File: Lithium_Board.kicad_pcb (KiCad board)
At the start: 6 copper layers, 80 x 67 mm, 120 parts, among them IC1 BQ25750RRVR, IC2 MCP1792T-3302H_DB, IC4 STM32G0B1CBT6N, IC5 TCAN3414DR, IC6 BQ7694204PFBR, J1 XT30PW-M, J2 XT30PW-F, J3 XT30PW-M, J4 S3B-XH-SM4-TB_LF__SN_, J5 TSW-105-07-G-S, J6 Conn_01x06, J7 Conn_01x04, Q1 SIR870ADP-T1-GE3, Q10 MMBT5551LT1G, Q2 SIR870ADP-T1-GE3, Q3 SIR870ADP-T1-GE3, Q4 SIR870ADP-T1-GE3, Q5 SIR870ADP-T1-GE3, Q6 SIR870ADP-T1-GE3, Q7 SIR870ADP-T1-GE3, Q8 SIR870ADP-T1-GE3

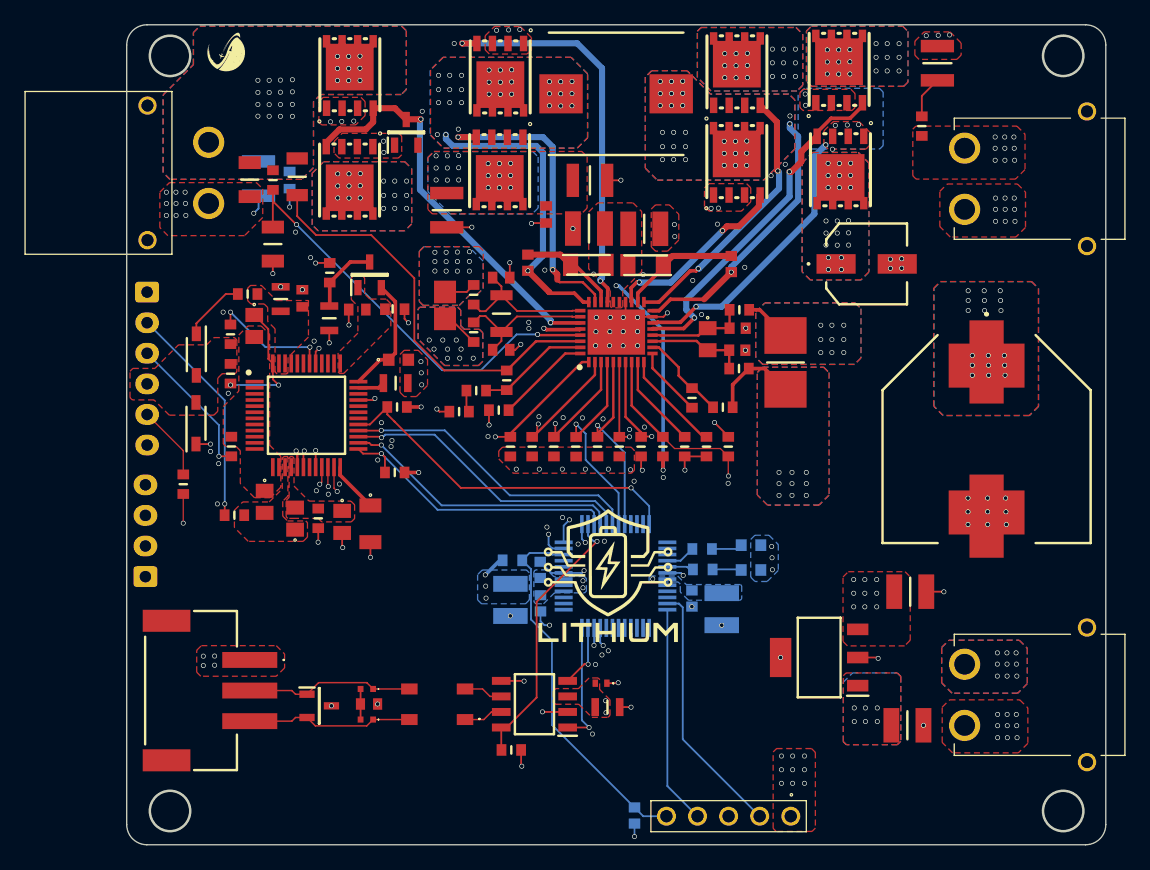
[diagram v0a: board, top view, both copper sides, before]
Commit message: Fixed Mounting Holes
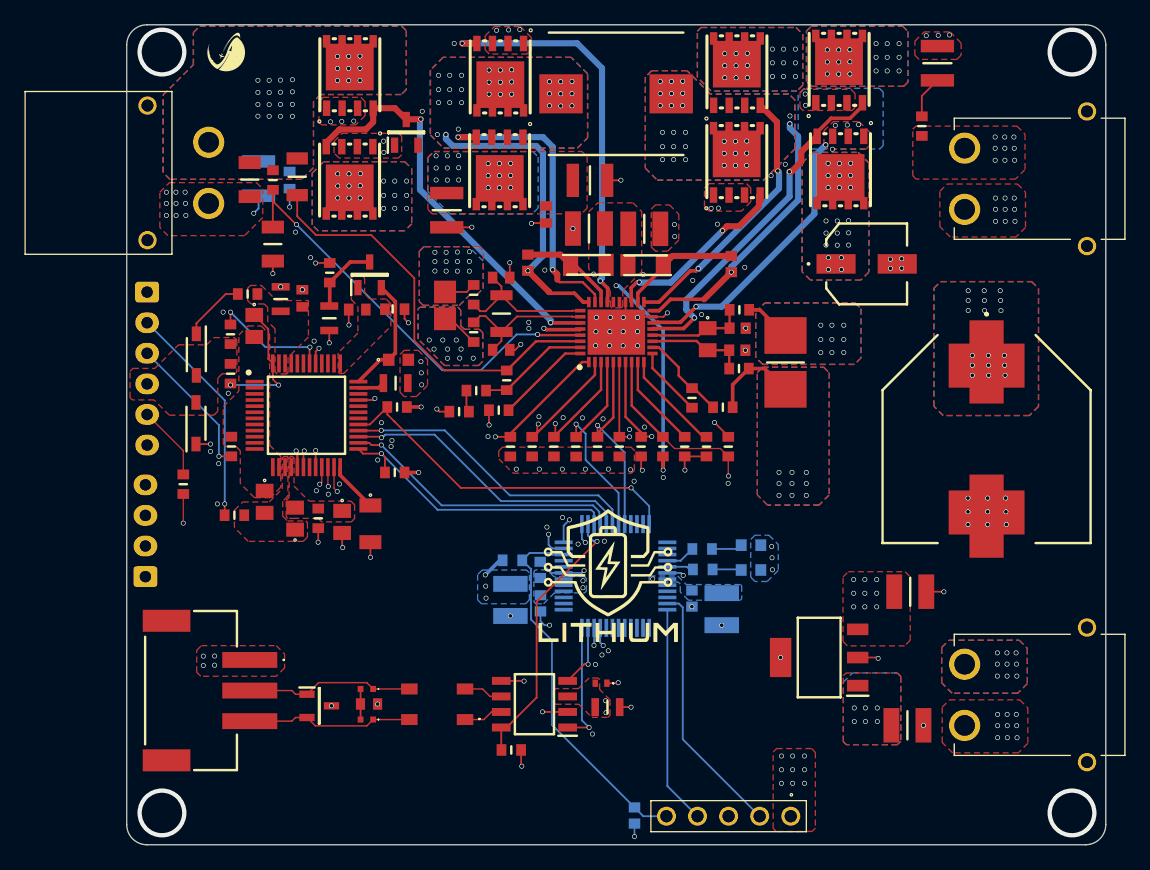
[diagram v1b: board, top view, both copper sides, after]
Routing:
- net GND: vias 171 -> 175
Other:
- outline, holes or cut-outs redrawn
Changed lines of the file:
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@@
 		(embedded_fonts no)
-	)
-	(gr_circle
-		(center 180.48 125.71)
-		(end 182.13 125.71)
-		(stroke
-			(width 0.2)
-			(type solid)
-		)
-		(fill no)
-		(layer "Edge.Cuts")
-	)
-	(gr_circle
-		(center 180.48 64.01)
-		(end 182.13 64.01)
-		(stroke
-			(width 0.2)
-			(type solid)
-		)
-		(fill no)
-		(layer "Edge.Cuts")
 	)
 	(gr_arc
@@
 		(layer "Edge.Cuts")
 	)
-	(gr_circle
-		(center 107.5 64.01)
-		(end 109.15 64.01)
-		(stroke
-			(width 0.2)
-			(type solid)
-		)
-		(fill no)
-		(layer "Edge.Cuts")
-	)
 	(gr_arc
 		(start 105.61 128.47)
@@
 			(type default)
 		)
-		(layer "Edge.Cuts")
-	)
-	(gr_circle
-		(center 107.5 125.71)
-		(end 109.15 125.71)
-		(stroke
-			(width 0.2)
-			(type solid)
-		)
-		(fill no)
 		(layer "Edge.Cuts")
 	)
@@
 	)
 	(via
+		(at 181.2 125.87)
+		(size 4)
+		(drill 3.3)
+		(layers "F.Cu" "B.Cu")
+		(free yes)
+		(tenting none)
+		(net 1)
+	)
+	(via
 		(at 176.48 75.63)
 		(size 0.4)
@@
 	)
 	(via
+		(at 106.84 63.7)
+		(size 4)
+		(drill 3.3)
+		(layers "F.Cu" "B.Cu")
+		(free yes)
+		(tenting none)
+		(net 1)
+	)
+	(via
 		(at 175.745 77.53)
 		(size 0.4)
@@
 	)
 	(via
+		(at 106.84 125.87)
+		(size 4)
+		(drill 3.3)
+		(layers "F.Cu" "B.Cu")
+		(free yes)
+		(tenting none)
+		(net 1)
+	)
+	(via
 		(at 158.151205 68.920096)
 		(size 0.4)
@@
 		(net 1)
 	)
+	(via
+		(at 181.2 63.7)
+		(size 4)
+		(drill 3.3)
+		(layers "F.Cu" "B.Cu")
+		(free yes)
+		(tenting none)
+		(net 1)
+	)

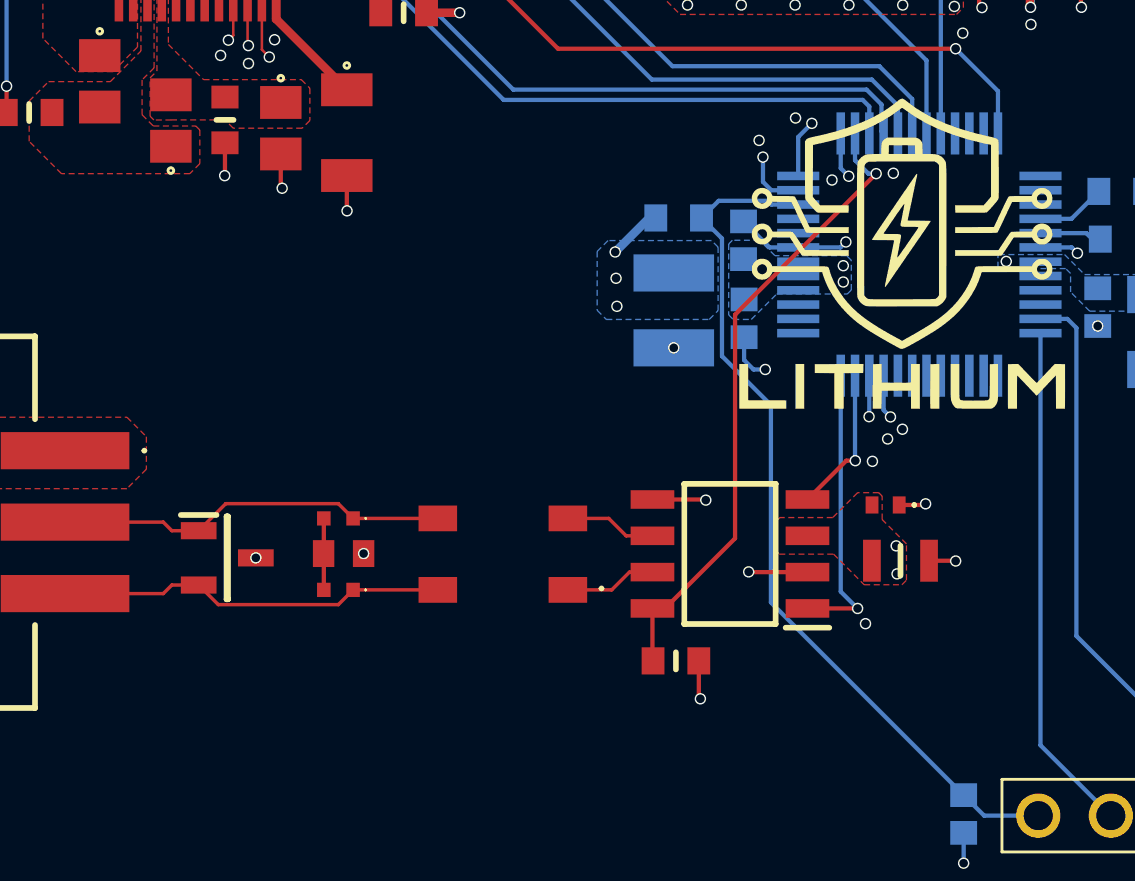
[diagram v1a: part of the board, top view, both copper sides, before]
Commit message: Fixed Items Not in Stock
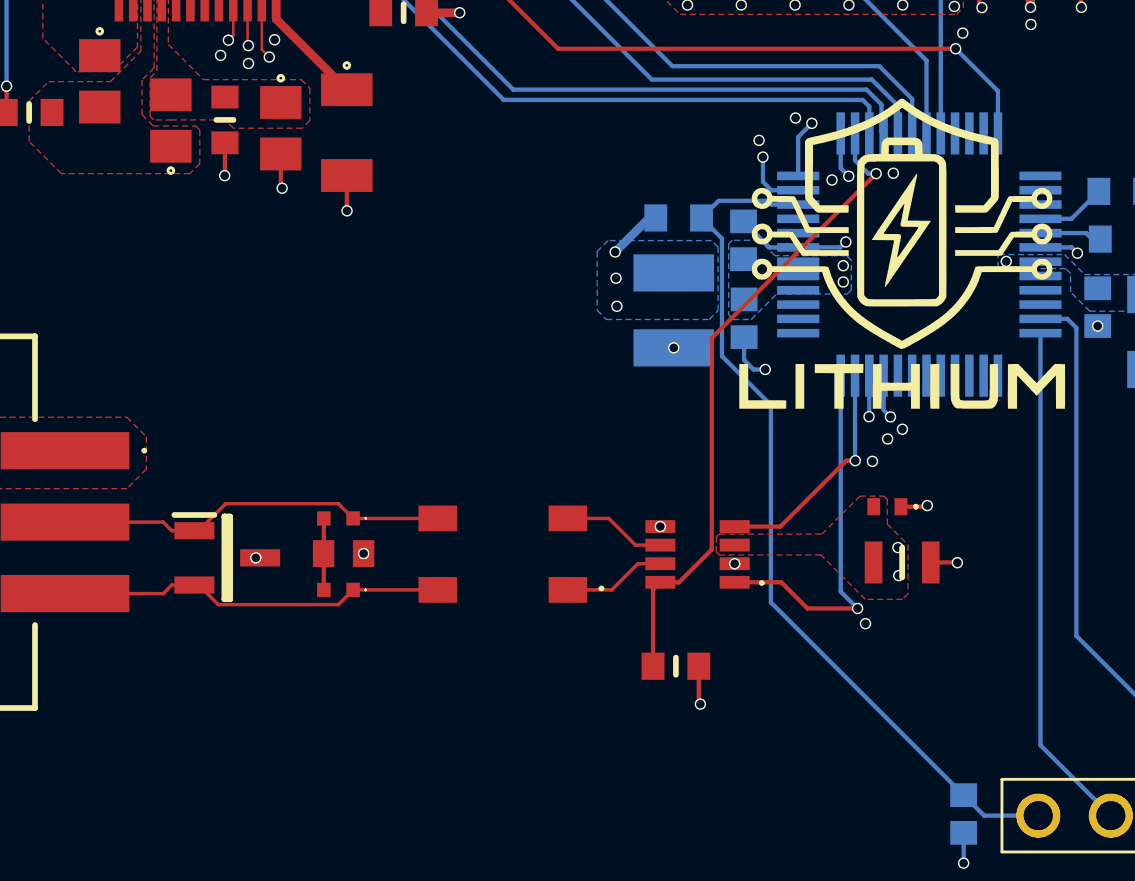
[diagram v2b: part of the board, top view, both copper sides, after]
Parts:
- removed IC5: TCAN3414DR, TCAN3414DR:SOIC127P600X175-8N
- added IC3: TCAN3414DDFR, TCAN3414DDFR:INA190A2NDDFREP, F.Cu at (136.1, 117.0)
- D1: value CDSOT23-T24CAN -> ESDCAN24-2BLY; footprint CDSOT23-T24CAN:SOT95P230X117-3N -> ESDCAN24-2BLY:SOT95P255X125-3N
- IC4: value STM32G0B1CBT6N -> STM32G0B1CET6N
- moved R35 0.19 mm to (135.4, 120.9)
- moved C25 0.08 mm to (142.8, 115.3)
- moved C26 0.08 mm to (143.3, 117.3)
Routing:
- net GND: track 61.2 -> 57.3 mm
- net FDCAN_RX: track 5.21 -> 8.15 mm
- net FDCAN_TX: track 10.1 -> 13.1 mm

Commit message: New BOM+GRB
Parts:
- IC4: footprint STM32G0B1CBT6N:QFP50P900X900X160-48N -> STM32G0B1CET6N:QFP50P900X900X160-48N
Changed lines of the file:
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@@
 		(tags "TVS Diode (Bi-directional)")
 		(property "Reference" "D1"
-			(at 0 0 -0)
+			(at 0 0 0)
 			(layer "B.SilkS")
 			(effects
@@
 		)
 		(fp_text user "${REFERENCE}"
-			(at 0 0 -0)
+			(at 0 0 0)
 			(layer "B.Fab")
 			(effects
@@
 		(tags "Integrated Circuit")
 		(property "Reference" "IC3"
-			(at 0 0 -0)
+			(at 0 0 0)
 			(layer "B.SilkS")
 			(effects
@@
 		)
 		(fp_text user "${REFERENCE}"
-			(at 0 0 -0)
+			(at 0 0 0)
 			(layer "B.Fab")
 			(effects
@@
 		)
 	)
-	(footprint "STM32G0B1CBT6N:QFP50P900X900X160-48N"
+	(footprint "STM32G0B1CET6N:QFP50P900X900X160-48N"
 		(layer "B.Cu")
 		(at 143.9 106.509999)
-		(descr "LQFP48 package information (5B)-1")
+		(descr "ANT1204F007R0870A")
 		(tags "Integrated Circuit")
 		(property "Reference" "IC4"
@@
 		)
 		(embedded_fonts no)
-		(model "${KIPRJMOD}/Lithium_Footprints/LIB_STM32G0B1CBT6N/STM32G0B1CBT6N/3D/STM32G0B1CBT6N.stp"
+		(model "STM32G0B1CET6N.stp"
 			(offset
 				(xyz 0 0 0)

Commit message: BOM Fixed+CS Fixed
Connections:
- IC4 pad 24: BQ2_CS -> unconnected-(IC4-PB12-Pad24)
- IC4 pad 37: unconnected-(IC4-PA15-Pad37) -> BQ2_CS
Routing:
- net BQ2_CS: track 29.5 -> 40.2 mm
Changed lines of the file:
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@@
 	(net 113 "unconnected-(IC4-PA11_[PA9]-Pad33)")
 	(net 114 "LED2_GREEN")
-	(net 115 "unconnected-(IC4-PA15-Pad37)")
+	(net 115 "unconnected-(IC4-PB12-Pad24)")
 	(net 116 "LED1_RED")
 	(net 117 "unconnected-(IC4-PD0-Pad38)")
@@
 			(size 0.3 1.475)
 			(layers "B.Cu" "B.Mask" "B.Paste")
-			(net 55 "BQ2_CS")
+			(net 115 "unconnected-(IC4-PB12-Pad24)")
 			(pinfunction "PB12")
-			(pintype "passive")
+			(pintype "passive+no_connect")
 		)
 		(pad "25" smd rect
@@
 			(size 0.3 1.475)
 			(layers "B.Cu" "B.Mask" "B.Paste")
-			(net 115 "unconnected-(IC4-PA15-Pad37)")
+			(net 55 "BQ2_CS")
 			(pinfunction "PA15")
-			(pintype "passive+no_connect")
+			(pintype "passive")
 		)
 		(pad "38" smd rect
@@
 	)
 	(segment
+		(start 148.613 109.8)
+		(end 147.663 110.75)
+		(width 0.15)
+		(layer "F.Cu")
+		(net 55)
+	)
+	(segment
 		(start 145.17 99.31)
 		(end 131.26 99.31)
@@
 	)
 	(segment
+		(start 148.613 102.753)
+		(end 148.613 109.8)
+		(width 0.15)
+		(layer "F.Cu")
+		(net 55)
+	)
+	(segment
+		(start 145.17 99.31)
+		(end 148.613 102.753)
+		(width 0.15)
+		(layer "F.Cu")
+		(net 55)
+	)
+	(segment
 		(start 131.26 99.31)
 		(end 125.84 93.89)
@@
 	)
 	(via
-		(at 145.17 99.31)
+		(at 147.663 110.75)
 		(size 0.4)
 		(drill 0.3)
 		(layers "F.Cu" "B.Cu")
-		(tenting front back)
 		(net 55)
 	)
 	(segment
-		(start 146.65 102.271999)
-		(end 146.65 100.79)
+		(start 146.652001 110.75)
+		(end 146.65 110.747999)
 		(width 0.15)
 		(layer "B.Cu")
@@
 	)
 	(segment
-		(start 146.65 100.79)
-		(end 145.17 99.31)
+		(start 147.663 110.75)
+		(end 146.652001 110.75)
 		(width 0.15)
 		(layer "B.Cu")

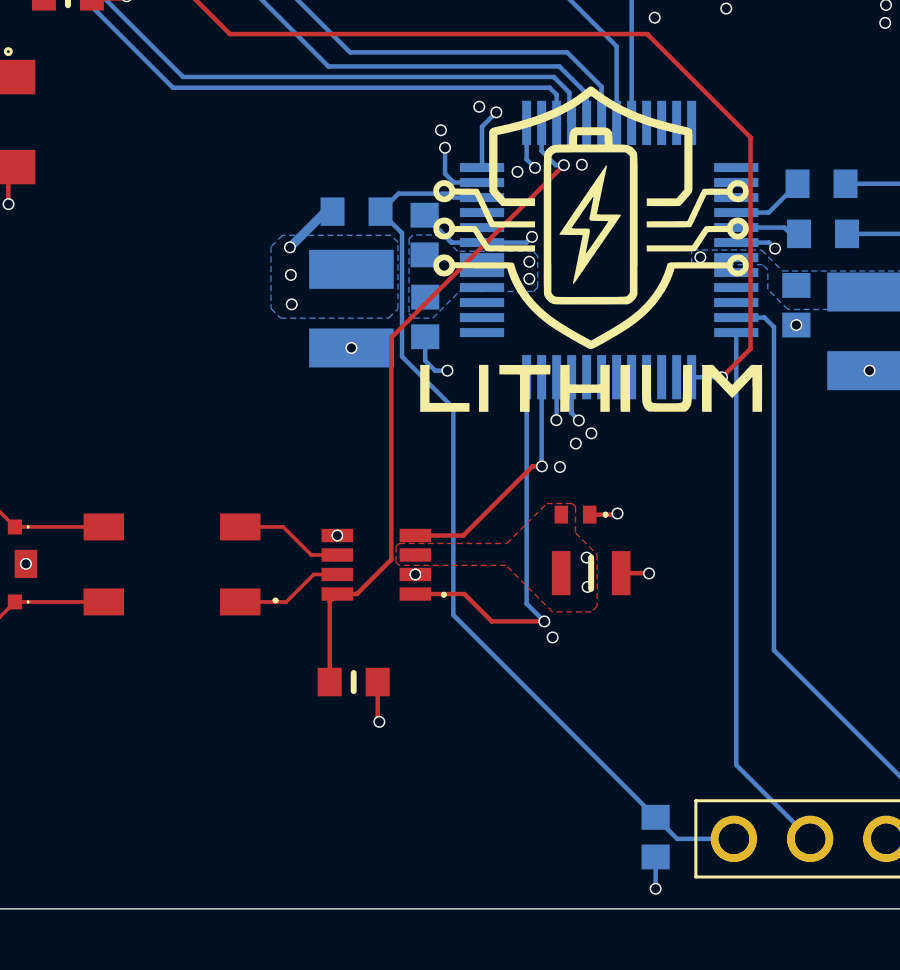
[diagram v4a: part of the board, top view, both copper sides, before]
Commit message: NRST+Polygon Fixed
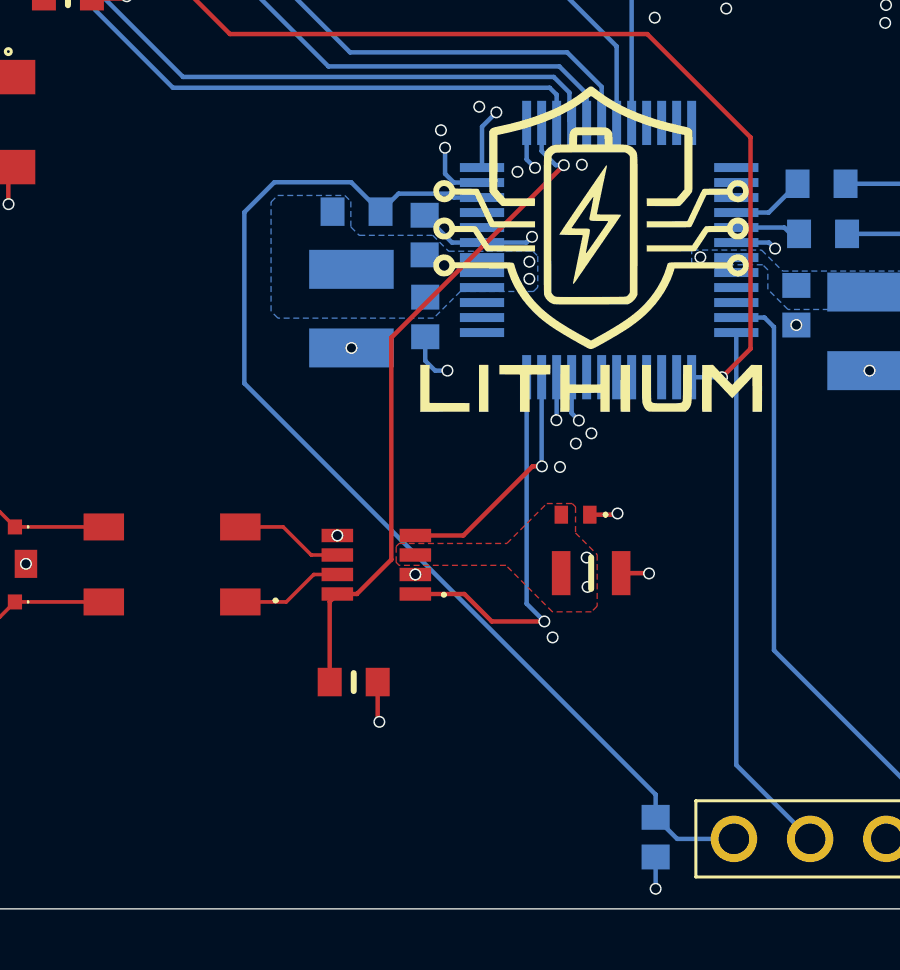
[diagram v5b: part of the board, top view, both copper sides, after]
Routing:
- net NRST: track 30.6 -> 37.8 mm
- net +3V3: track 4.24 -> 2.33 mm, vias 34 -> 31
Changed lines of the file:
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@@
 	)
 	(via
-		(at 133.32 108.32)
-		(size 0.4)
-		(drill 0.3)
-		(layers "F.Cu" "B.Cu")
-		(free yes)
-		(tenting front back)
-		(net 12)
-	)
-	(via
 		(at 163.36 106.8)
 		(size 0.4)
@@
 	)
 	(via
-		(at 133.26 106.42)
-		(size 0.4)
-		(drill 0.3)
-		(layers "F.Cu" "B.Cu")
-		(free yes)
-		(tenting front back)
-		(net 12)
-	)
-	(via
 		(at 137.672 97.78)
 		(size 0.4)
@@
 	)
 	(via
-		(at 133.29 107.34)
-		(size 0.4)
-		(drill 0.3)
-		(layers "F.Cu" "B.Cu")
-		(free yes)
-		(tenting front back)
-		(net 12)
-	)
-	(via
 		(at 158.37 121.22)
 		(size 0.4)
@@
 	)
 	(segment
-		(start 134.45 105.23)
-		(end 133.26 106.42)
-		(width 0.3)
-		(layer "B.Cu")
-		(net 12)
-	)
-	(segment
-		(start 134.68 105.23)
-		(end 134.45 105.23)
-		(width 0.3)
-		(layer "B.Cu")
-		(net 12)
-	)
-	(segment
 		(start 154.79 89.56)
 		(end 156.088225 89.56)
@@
 	)
 	(segment
-		(start 138.707166 118.677166)
-		(end 138.707166 111.774165)
+		(start 148.06 126.1375)
+		(end 146.1675 126.1375)
 		(width 0.15)
 		(layer "B.Cu")
@@
 	)
 	(segment
-		(start 136.996 110.062999)
-		(end 136.996 105.946)
+		(start 145.45 124.661834)
+		(end 145.45 125.42)
 		(width 0.15)
 		(layer "B.Cu")
@@
 	)
 	(segment
-		(start 138.707166 111.774165)
-		(end 136.996 110.062999)
+		(start 131.74 110.951834)
+		(end 145.45 124.661834)
 		(width 0.15)
 		(layer "B.Cu")
@@
 	)
 	(segment
-		(start 148.06 126.1375)
-		(end 146.1675 126.1375)
+		(start 136.28 105.23)
+		(end 136.88 104.63)
 		(width 0.15)
 		(layer "B.Cu")
@@
 	)
 	(segment
-		(start 136.28 105.23)
-		(end 136.88 104.63)
+		(start 146.1675 126.1375)
+		(end 145.45 125.42)
 		(width 0.15)
 		(layer "B.Cu")
@@
 	)
 	(segment
-		(start 146.1675 126.1375)
-		(end 145.45 125.42)
+		(start 136.88 104.63)
+		(end 138.592501 104.63)
 		(width 0.15)
 		(layer "B.Cu")
@@
 	)
 	(segment
-		(start 145.45 125.42)
-		(end 138.707166 118.677166)
+		(start 131.74 105.25)
+		(end 131.74 110.951834)
 		(width 0.15)
 		(layer "B.Cu")
@@
 	)
 	(segment
-		(start 136.88 104.63)
-		(end 138.592501 104.63)
+		(start 135.3 104.25)
+		(end 132.74 104.25)
 		(width 0.15)
 		(layer "B.Cu")
@@
 	)
 	(segment
-		(start 136.996 105.946)
-		(end 136.28 105.23)
+		(start 132.74 104.25)
+		(end 131.74 105.25)
 		(width 0.15)
 		(layer "B.Cu")
@@
 	)
 	(segment
+		(start 136.28 105.23)
+		(end 135.3 104.25)
+		(width 0.15)
+		(layer "B.Cu")
+		(net 15)
+	)
+	(segment
 		(start 168.93 67.28)
 		(end 170.2 66.01)
@@
 	)
 	(zone
+		(net 12)
+		(net_name "+3V3")
+		(layer "B.Cu")
+		(hatch edge 0.5)
+		(priority 15)
+		(connect_pads yes
+			(clearance 0.2)
+		)
+		(min_thickness 0.25)
+		(filled_areas_thickness no)
+		(fill yes
+			(thermal_gap 0.5)
+			(thermal_bridge_width 0.5)
+		)
+		(polygon
+			(pts
+				(xy 141.36 106.55) (xy 141.52 106.71) (xy 141.52 107.75) (xy 141.38 107.89) (xy 138.94 107.89) (xy 138.05 108.78)
+				(xy 132.86 108.78) (xy 132.63 108.55) (xy 132.63 104.91) (xy 132.85 104.69) (xy 135.09 104.69) (xy 135.29 104.89)
+				(xy 135.29 105.74) (xy 135.57 106.02) (xy 138.02 106.02) (xy 138.55 106.55)
+			)
+		)
+	)
+	(zone
 		(net 35)
 		(net_name "BQ_BATSRC")
@@
 			)
 		)
-	)
-	(zone
-		(net 12)
-		(net_name "+3V3")
-		(layer "B.Cu")
-		(hatch edge 0.5)
-		(priority 28)
-		(connect_pads yes
-			(clearance 0.2)
-		)
-		(min_thickness 0.25)
-		(filled_areas_thickness no)
-		(fill yes
-			(thermal_gap 0.5)
-			(thermal_bridge_width 0.5)
-		)
-		(polygon
-			(pts
-				(xy 133.01 106.02) (xy 132.63 106.4) (xy 132.63 108.46) (xy 132.95 108.78) (xy 136.55 108.78) (xy 136.86 108.47)
-				(xy 136.86 106.25) (xy 136.63 106.02)
-			)
-		)
-	)
-	(zone
-		(net 12)
-		(net_name "+3V3")
-		(layer "B.Cu")
-		(hatch edge 0.5)
-		(priority 29)
-		(connect_pads yes
-			(clearance 0.2)
-		)
-		(min_thickness 0.25)
-		(filled_areas_thickness no)
-		(fill yes
-			(thermal_gap 0.5)
-			(thermal_bridge_width 0.5)
-		)
-		(polygon
-			(pts
-				(xy 137.36 106.009999) (xy 137.23 106.139999) (xy 137.23 108.62) (xy 137.39 108.78) (xy 138.02 108.78)
-				(xy 138.91 107.89) (xy 141.38 107.89) (xy 141.52 107.75) (xy 141.52 106.71) (xy 141.36 106.55) (xy 138.85 106.55)
-				(xy 138.309999 106.009999)
-			)
-		)
